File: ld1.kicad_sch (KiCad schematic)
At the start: 42 parts, among them J1 ENCODER, J2 PROG, J3 MISC, J4 POWER, J5 5V, J6 GND, J7 3V3, J8 GPS+OLED, SW3 KLS7-KL-02-N-0-0, U1 E22-400M30S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

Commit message: Fixed pinsocket connector, fixed missing connectors footprints
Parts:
- J2, J5, J6, J7: footprint (none) -> Connector_PinHeader_2.54mm:PinHeader_1x02_P2.54mm_Vertical
- J4: footprint Connector_PinSocket_2.54mm:PinSocket_1x03_P2.54mm_Vertical -> Connector_PinHeader_2.54mm:PinHeader_1x03_P2.54mm_Vertical
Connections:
- net RX0: now also J2.2 (Pin_2); no longer J2.1 (Pin_1)
- net TX0: now also J2.1 (Pin_1); no longer J2.2 (Pin_2)
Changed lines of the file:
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@@
 			)
 		)
-		(property "Footprint" ""
+		(property "Footprint" "Connector_PinHeader_2.54mm:PinHeader_1x02_P2.54mm_Vertical"
 			(at 143.51 97.79 0)
 			(effects
@@
 			)
 		)
-		(property "Footprint" ""
+		(property "Footprint" "Connector_PinHeader_2.54mm:PinHeader_1x02_P2.54mm_Vertical"
 			(at 143.51 104.14 0)
 			(effects
@@
 			)
 		)
-		(property "Footprint" "Connector_PinSocket_2.54mm:PinSocket_1x03_P2.54mm_Vertical"
+		(property "Footprint" "Connector_PinHeader_2.54mm:PinHeader_1x03_P2.54mm_Vertical"
 			(at 143.51 76.2 0)
 			(effects
@@
 	)
 	(symbol
-		(lib_id "Connector:Conn_01x02_Pin")
-		(at 143.51 114.3 180)
-		(unit 1)
-		(exclude_from_sim no)
-		(in_bom yes)
-		(on_board yes)
-		(dnp no)
-		(fields_autoplaced yes)
-		(property "Reference" "J2"
-			(at 144.78 111.7599 0)
-			(effects
-				(font
-					(size 1.27 1.27)
-				)
-				(justify right)
-			)
-		)
-		(property "Value" "PROG"
-			(at 144.78 114.2999 0)
-			(effects
-				(font
-					(size 1.27 1.27)
-				)
-				(justify right)
-			)
-		)
-		(property "Footprint" ""
-			(at 143.51 114.3 0)
-			(effects
-				(font
-					(size 1.27 1.27)
-				)
-				(hide yes)
-			)
-		)
-		(property "Datasheet" "~"
-			(at 143.51 114.3 0)
-			(effects
-				(font
-					(size 1.27 1.27)
-				)
-				(hide yes)
-			)
-		)
-		(property "Description" "Generic connector, single row, 01x02, script generated"
-			(at 143.51 114.3 0)
-			(effects
-				(font
-					(size 1.27 1.27)
-				)
-				(hide yes)
-			)
-		)
-		(pin "2"
-		)
-		(pin "1"
-		)
-		(instances
-			(project "ld1"
-				(path "/b32b136d-bf21-4725-82bc-3d3551c16114"
-					(reference "J2")
-					(unit 1)
-				)
-			)
-		)
-	)
-	(symbol
 		(lib_id "Device:R")
 		(at 274.32 128.27 90)
@@
 			)
 		)
-		(property "Footprint" ""
+		(property "Footprint" "Connector_PinHeader_2.54mm:PinHeader_1x02_P2.54mm_Vertical"
 			(at 143.51 91.44 0)
 			(effects
@@
 					(unit 1)
 				)
+			)
+		)
+	)
+	(symbol
+		(lib_id "Connector:Conn_01x02_Pin")
+		(at 143.51 111.76 0)
+		(mirror y)
+		(unit 1)
+		(exclude_from_sim no)
+		(in_bom yes)
+		(on_board yes)
+		(dnp no)
+		(property "Reference" "J2"
+			(at 144.78 114.3001 0)
+			(effects
+				(font
+					(size 1.27 1.27)
+				)
+				(justify right)
+			)
+		)
+		(property "Value" "PROG"
+			(at 144.78 111.7601 0)
+			(effects
+				(font
+					(size 1.27 1.27)
+				)
+				(justify right)
+			)
+		)
+		(property "Footprint" "Connector_PinHeader_2.54mm:PinHeader_1x02_P2.54mm_Vertical"
+			(at 143.51 111.76 0)
+			(effects
+				(font
+					(size 1.27 1.27)
+				)
+				(hide yes)
+			)
+		)
+		(property "Datasheet" "~"
+			(at 143.51 111.76 0)
+			(effects
+				(font
+					(size 1.27 1.27)
+				)
+				(hide yes)
+			)
+		)
+		(property "Description" "Generic connector, single row, 01x02, script generated"
+			(at 143.51 111.76 0)
+			(effects
+				(font
+					(size 1.27 1.27)
+				)
+				(hide yes)
+			)
+		)
+		(pin "2"
+		)
+		(pin "1"
+		)
+		(instances
+			(project "ld1"
+				(path "/b32b136d-bf21-4725-82bc-3d3551c16114"
+					(reference "J2")
+					(unit 1)
+				)

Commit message: Added GND pin for better return current path when using underlying board
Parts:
- added J9: GND, Connector_PinHeader_2.54mm:PinHeader_1x01_P2.54mm_Vertical, symbol Connector:Conn_01x01_Pin
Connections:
- net GND: now also J9.1 (Pin_1)
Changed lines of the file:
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@@
 	(wire
 		(pts
+			(xy 133.35 168.91) (xy 135.89 168.91)
+		)
+		(stroke
+			(width 0)
+			(type default)
+		)
+	)
+	(wire
+		(pts
 			(xy 270.51 147.32) (xy 269.24 147.32)
 		)
@@
 	(wire
 		(pts
+			(xy 133.35 171.45) (xy 133.35 168.91)
+		)
+		(stroke
+			(width 0)
+			(type default)
+		)
+	)
+	(wire
+		(pts
 			(xy 165.1 26.67) (xy 165.1 29.21)
 		)
@@
 	)
 	(symbol
+		(lib_id "power:GND")
+		(at 133.35 171.45 0)
+		(unit 1)
+		(exclude_from_sim no)
+		(in_bom yes)
+		(on_board yes)
+		(dnp no)
+		(property "Reference" "#PWR047"
+			(at 133.35 177.8 0)
+			(effects
+				(font
+					(size 1.27 1.27)
+				)
+				(hide yes)
+			)
+		)
+		(property "Value" "GND"
+			(at 133.35 175.768 0)
+			(effects
+				(font
+					(size 1.27 1.27)
+				)
+			)
+		)
+		(property "Footprint" ""
+			(at 133.35 171.45 0)
+			(effects
+				(font
+					(size 1.27 1.27)
+				)
+				(hide yes)
+			)
+		)
+		(property "Datasheet" ""
+			(at 133.35 171.45 0)
+			(effects
+				(font
+					(size 1.27 1.27)
+				)
+				(hide yes)
+			)
+		)
+		(property "Description" "Power symbol creates a global label with name \"GND\" , ground"
+			(at 133.35 171.45 0)
+			(effects
+				(font
+					(size 1.27 1.27)
+				)
+				(hide yes)
+			)
+		)
+		(pin "1"
+		)
+		(instances
+			(project "ld1"
+				(path "/b32b136d-bf21-4725-82bc-3d3551c16114"
+					(reference "#PWR047")
+					(unit 1)
+				)
+			)
+		)
+	)
+	(symbol
 		(lib_id "Device:LED")
 		(at 71.12 163.83 90)
@@
 					(unit 1)
 				)
+			)
+		)
+	)
+	(symbol
+		(lib_id "Connector:Conn_01x01_Pin")
+		(at 140.97 168.91 180)
+		(unit 1)
+		(exclude_from_sim no)
+		(in_bom yes)
+		(on_board yes)
+		(dnp no)
+		(property "Reference" "J9"
+			(at 144.272 167.64 0)
+			(effects
+				(font
+					(size 1.27 1.27)
+				)
+			)
+		)
+		(property "Value" "GND"
+			(at 144.272 170.18 0)
+			(effects
+				(font
+					(size 1.27 1.27)
+				)
+			)
+		)
+		(property "Footprint" "Connector_PinHeader_2.54mm:PinHeader_1x01_P2.54mm_Vertical"
+			(at 140.97 168.91 0)
+			(effects
+				(font
+					(size 1.27 1.27)
+				)
+				(hide yes)
+			)
+		)
+		(property "Datasheet" "~"
+			(at 140.97 168.91 0)
+			(effects
+				(font
+					(size 1.27 1.27)
+				)
+				(hide yes)
+			)
+		)
+		(property "Description" "Generic connector, single row, 01x01, script generated"
+			(at 140.97 168.91 0)
+			(effects
+				(font
+					(size 1.27 1.27)
+				)
+				(hide yes)
+			)
+		)
+		(pin "1"
+		)
+		(instances
+			(project "ld1"
+				(path "/b32b136d-bf21-4725-82bc-3d3551c16114"
+					(reference "J9")
+					(unit 1)
+				)

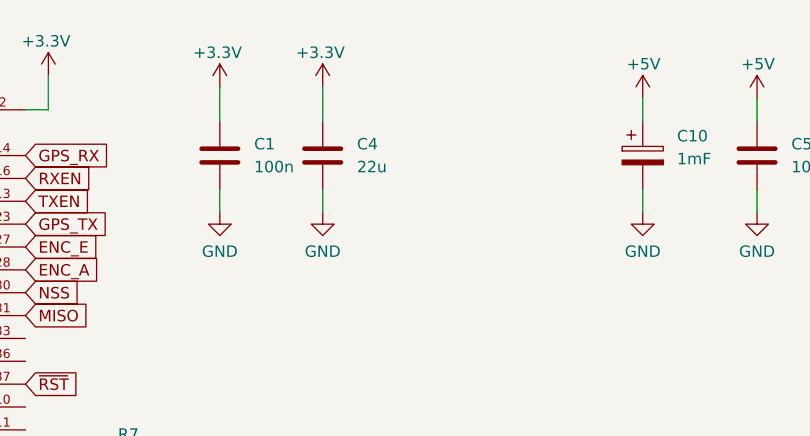
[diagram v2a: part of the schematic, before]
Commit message: Added 100u caps
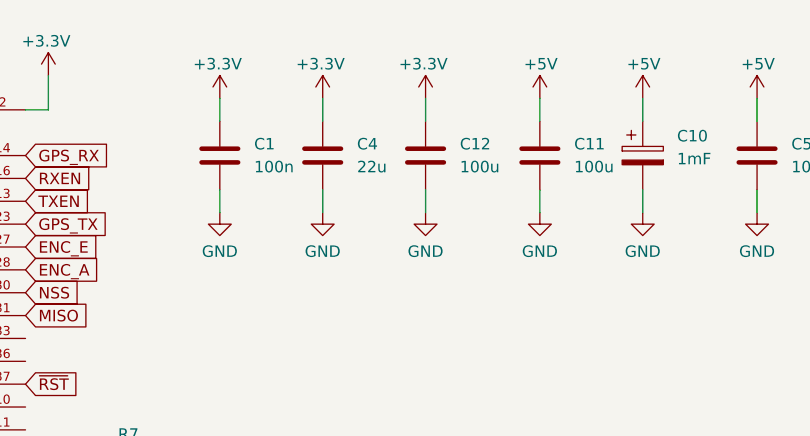
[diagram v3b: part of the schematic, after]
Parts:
- added C11, C12: 100u, Capacitor_SMD:C_1206_3216Metric_Pad1.33x1.80mm_HandSolder, symbol Device:C
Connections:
- net +3.3V: now also C12.1
- net +5V: now also C11.1
- net GND: now also C11.2, C12.2
